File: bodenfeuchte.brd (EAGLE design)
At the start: 201.9 x 33 mm, 16 parts, among them IC1 74HC14D, IC2 HT7333

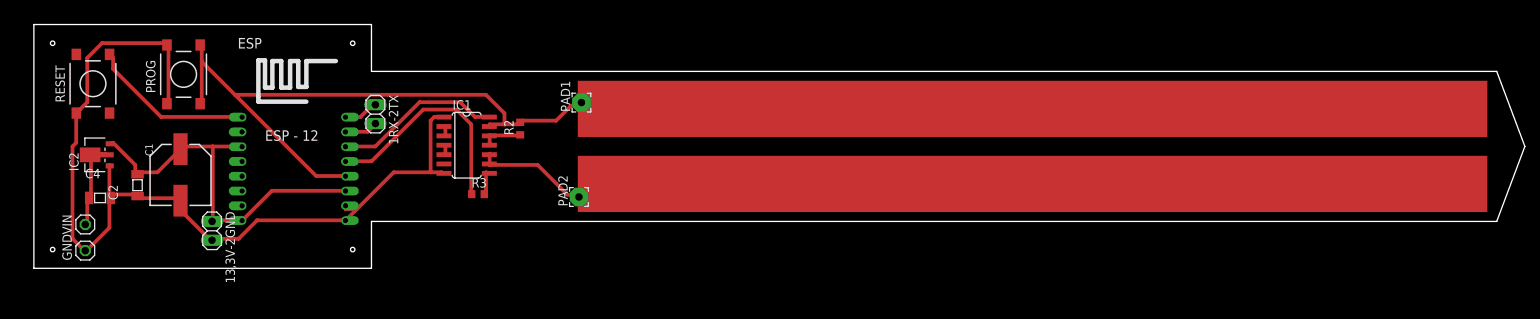
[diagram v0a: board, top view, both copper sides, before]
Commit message: - new version of board - added trim resistor (500KΩ) to adjust cap. frequency (works like a charm) - better routing - made first real prototype board (self etching) - board works great with Zentris software
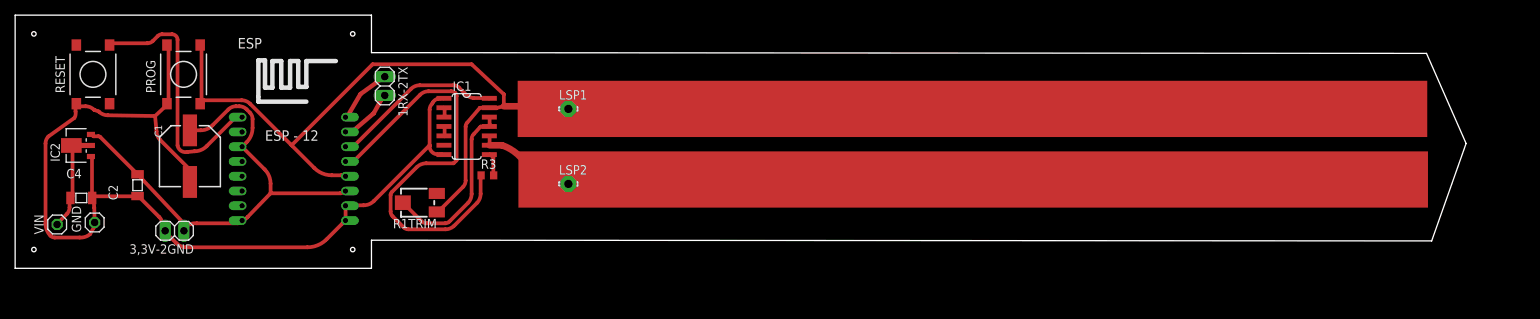
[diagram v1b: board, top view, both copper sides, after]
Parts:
- removed 13,3V-2GND: (no value), pinhead:1X02
- removed PAD1, PAD2: (no value), wirepad:2,54/1,0
- removed R2: ca 100k, rcl:R0603
- added 3,3V-2GND: (no value), pinhead:1X02
- added LSP1, LSP2: LSP11, solpad:LSP11
- added R1TRIM: 500K, rcl:RTRIM3374
- ESP: value (none) -> ESP12
- moved 1RX-2TX 4.02 mm to (48.8, 24.7)
- moved GND 4.02 mm to (9.50, 6.21)
- moved VIN 3.81 mm to (4.42, 5.94)
- moved IC2 2.84 mm to (6.61, 16.6)
- moved C1 2.84 mm to (22.4, 15.2)
- moved R3 2.84 mm to (62.7, 12.6)
- moved C4 2.54 mm to (7.69, 9.53)
- moved IC1 2.54 mm to (59.9, 19.2)
- moved RESET 1.27 mm to (9.27, 26.3)
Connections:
- net 3.3V: now also 3,3V-2GND.1; no longer 13,3V-2GND.1
- net GND: now also 3,3V-2GND.2; no longer 13,3V-2GND.2
- net N$7: now also LSP2.MP; no longer PAD2.1
- net N$8: now also R1TRIM.2; no longer R2.1
- net N$9: now also LSP1.MP, R1TRIM.1; no longer PAD1.1, R2.2
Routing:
- net N$11: track 30.2 -> 59.0 mm
- net N$8: track 5.56 -> 24.3 mm
- net 3.3V: track 51.7 -> 64.6 mm
- net N$4: track 22.3 -> 35.1 mm
- net N$9: track 86.9 -> 97.3 mm
- net GND: track 124.6 -> 134.7 mm
- net N$2: track 4.57 -> 7.61 mm
- net N$1: track 5.22 -> 7.82 mm
- net N$7: track 15.5 -> 13.7 mm
- net BIS6VVCC: track 12.4 -> 13.8 mm
- net N$3: track 22.8 -> 23.4 mm
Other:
- board size 201.9 x 33 mm -> 196.5 x 34.3 mm

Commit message: updated readme
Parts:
- renumbered 3,3V-2GND to GND-3.3V
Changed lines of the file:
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@@
 <layer number="19" name="Unrouted" color="6" fill="1" visible="yes" active="yes"/>
 <layer number="20" name="Dimension" color="15" fill="1" visible="yes" active="yes"/>
-<layer number="21" name="tPlace" color="7" fill="1" visible="no" active="yes"/>
-<layer number="22" name="bPlace" color="7" fill="1" visible="no" active="yes"/>
-<layer number="23" name="tOrigins" color="15" fill="1" visible="no" active="yes"/>
-<layer number="24" name="bOrigins" color="15" fill="1" visible="no" active="yes"/>
-<layer number="25" name="tNames" color="7" fill="1" visible="no" active="yes"/>
-<layer number="26" name="bNames" color="7" fill="1" visible="no" active="yes"/>
-<layer number="27" name="tValues" color="7" fill="1" visible="no" active="yes"/>
-<layer number="28" name="bValues" color="7" fill="1" visible="no" active="yes"/>
+<layer number="21" name="tPlace" color="7" fill="1" visible="yes" active="yes"/>
+<layer number="22" name="bPlace" color="7" fill="1" visible="yes" active="yes"/>
+<layer number="23" name="tOrigins" color="15" fill="1" visible="yes" active="yes"/>
+<layer number="24" name="bOrigins" color="15" fill="1" visible="yes" active="yes"/>
+<layer number="25" name="tNames" color="7" fill="1" visible="yes" active="yes"/>
+<layer number="26" name="bNames" color="7" fill="1" visible="yes" active="yes"/>
+<layer number="27" name="tValues" color="7" fill="1" visible="yes" active="yes"/>
+<layer number="28" name="bValues" color="7" fill="1" visible="yes" active="yes"/>
 <layer number="29" name="tStop" color="7" fill="3" visible="no" active="yes"/>
 <layer number="30" name="bStop" color="7" fill="6" visible="no" active="yes"/>
@@
 <layer number="45" name="Holes" color="7" fill="1" visible="yes" active="yes"/>
 <layer number="46" name="Milling" color="3" fill="1" visible="no" active="yes"/>
-<layer number="47" name="Measures" color="7" fill="1" visible="no" active="yes"/>
+<layer number="47" name="Measures" color="7" fill="1" visible="yes" active="yes"/>
 <layer number="48" name="Document" color="7" fill="1" visible="no" active="yes"/>
 <layer number="49" name="Reference" color="7" fill="1" visible="no" active="yes"/>
@@
 <element name="PROG" library="switch-tact" package="DTSM-6" value="DTSM-6" x="21.54" y="26.27" rot="R90"/>
 <element name="RESET" library="switch-tact" package="DTSM-6" value="DTSM-6" x="9.27" y="26.27" rot="R90"/>
-<element name="3,3V-2GND" library="pinhead" package="1X02" value="" x="20.32" y="5.08" rot="R180"/>
+<element name="GND-3.3V" library="pinhead" package="1X02" value="" x="20.32" y="5.08" rot="R180"/>
 <element name="LSP1" library="solpad" package="LSP11" value="LSP11" x="73.66" y="21.59"/>
 <element name="LSP2" library="solpad" package="LSP11" value="LSP11" x="73.66" y="11.43"/>
@@
 <contactref element="RESET" pad="1"/>
 <contactref element="PROG" pad="2"/>
-<contactref element="3,3V-2GND" pad="2"/>
+<contactref element="GND-3.3V" pad="2"/>
 <wire x1="9.43155625" y1="21.46124375" x2="10.0547125" y2="21.2380875" width="0.508" layer="1"/>
 <wire x1="9.43155625" y1="21.46124375" x2="8.26221875" y2="21.9456" width="0.508" layer="1" curve="45"/>
@@
 <contactref element="ESP" pad="GPIO2"/>
 <contactref element="ESP" pad="CH_PD"/>
-<contactref element="3,3V-2GND" pad="1"/>
+<contactref element="GND-3.3V" pad="1"/>
 <wire x1="15.0368" y1="13.0048" x2="10.26545" y2="17.77615" width="0.508" layer="1"/>
 <wire x1="10.26545" y1="17.77615" x2="10.010871875" y2="17.8816" width="0.508" layer="1" curve="45.000497"/>
